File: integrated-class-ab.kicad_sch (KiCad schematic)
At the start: 35 parts, among them U10 CSA230PASOT235, U5 SL9062D, U9 LT1794

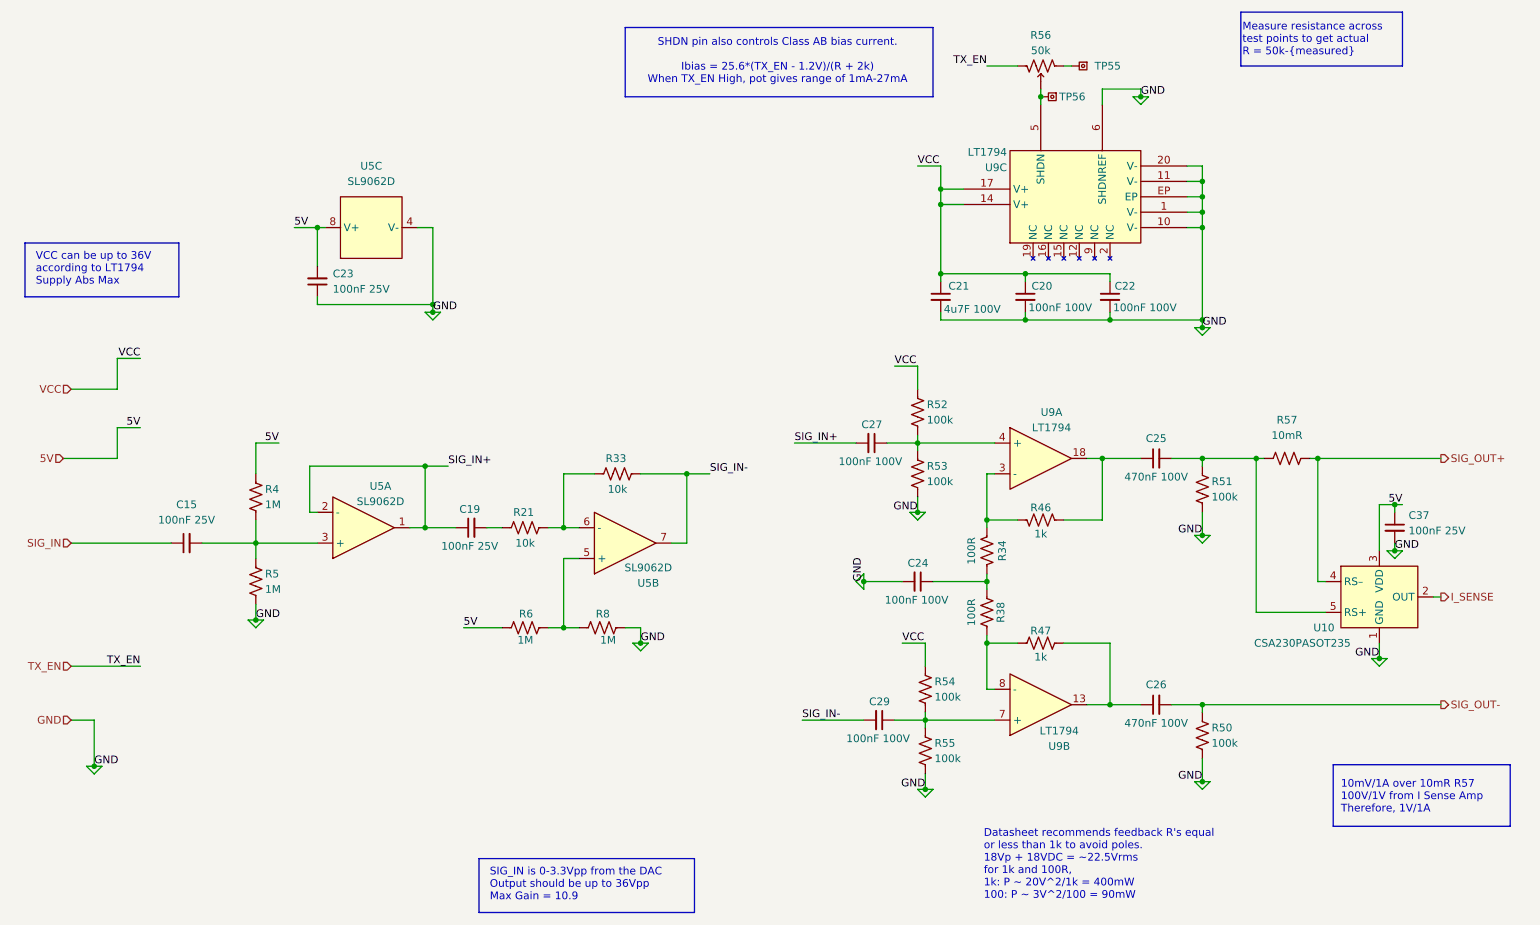
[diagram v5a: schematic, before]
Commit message: implementing feedback + added stepper driver
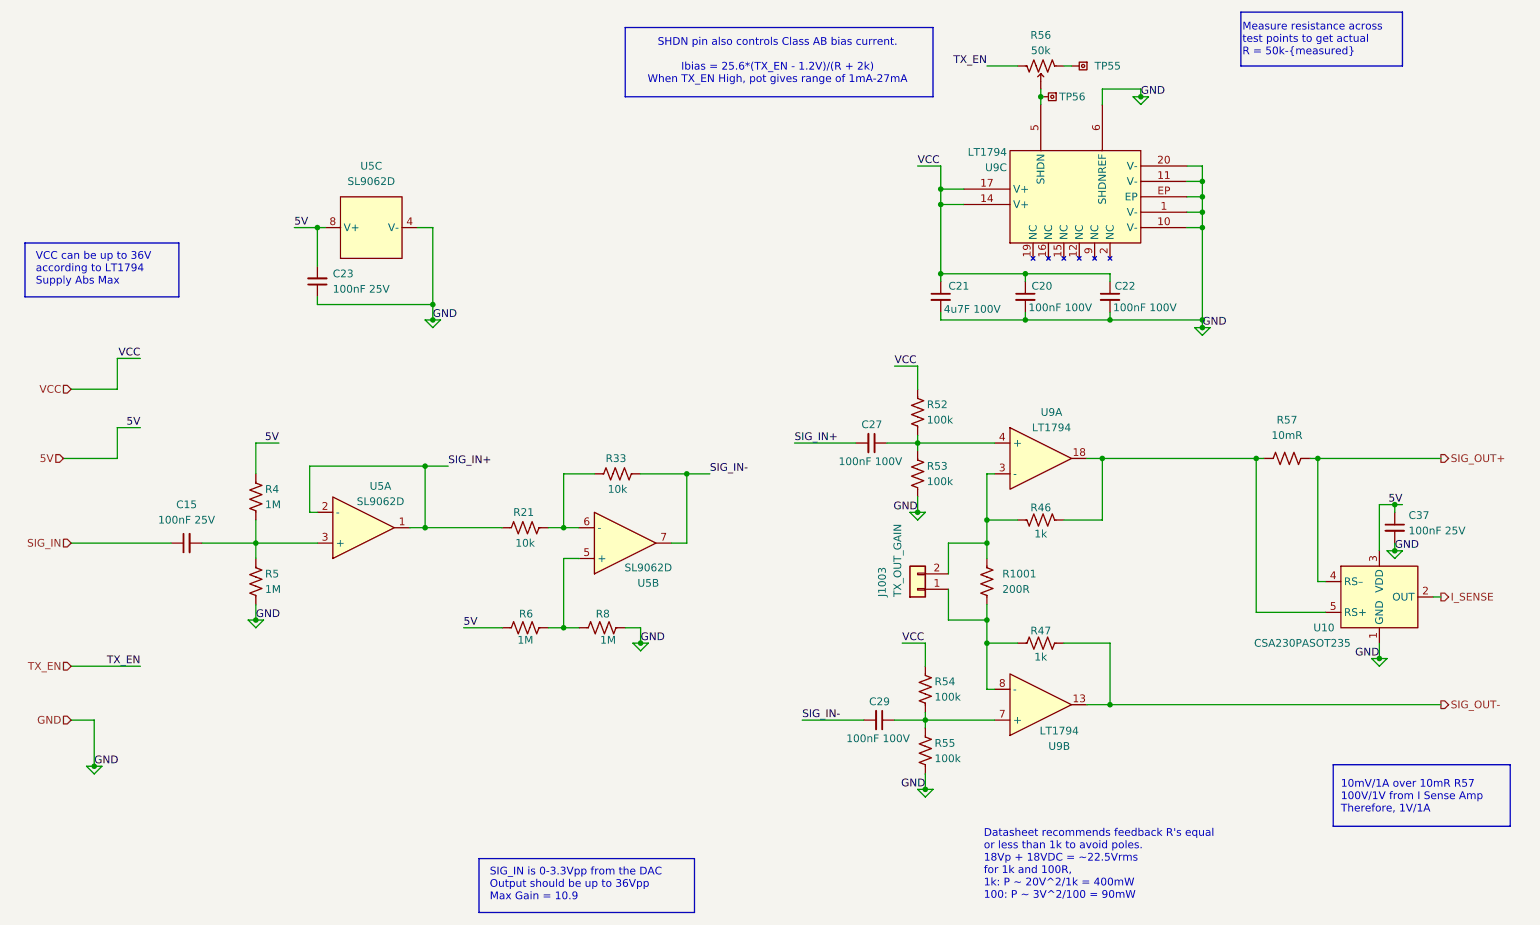
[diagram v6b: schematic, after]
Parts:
- removed C19: 100nF 25V, BR_Passives:C_0201_0603Metric-minimized, symbol BR_Capacitors_0201:C_0201_100nF_25V_X7R_10%
- removed C24: 100nF 100V, BR_Passives:C_0402_1005Metric-minimized, symbol BR_Capacitors_0402:C_0402_100nF_100V_X5R_20%
- removed C25, C26: 470nF 100V, BR_Passives:C_0805_2012Metric-minimized, symbol BR_Capacitors_0805:C_0805_470nF_100V_X7R_10%
- removed R34, R38: 100R, BR_Passives:R_0603_1608Metric, symbol BR_Resistors_0603:R_0603_100R
- removed R50, R51: 100k, BR_Passives:R_0201_0603Metric-minimized, symbol BR_Resistors_0201:R_0201_100k
- added J1003: TX_OUT_GAIN, BR_Connectors:PinHeader_1x02_P2.54mm_Vertical, symbol BR_Connectors_Header:Header_Socket_SIP_01x02_2.54mm_Vert_PTH
- added R1001: 200R, BR_Passives:C_0402_1005Metric-minimized, symbol BR_Resistors_0402:R_0402_200R
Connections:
- net SIG_IN+: now also R21.1
- net SIG_OUT-: now also R47.2, U9.13
- net at R47.1, U9.8 (-): now also J1003.1 (Pin_1), R1001.2
- net at R46.2, U9.3 (-): now also J1003.2 (Pin_2), R1001.1
- net at R46.1, U9.18: now also R57.1, U10.5 (RS+)

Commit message: completed feedback from review + reannotated sheets
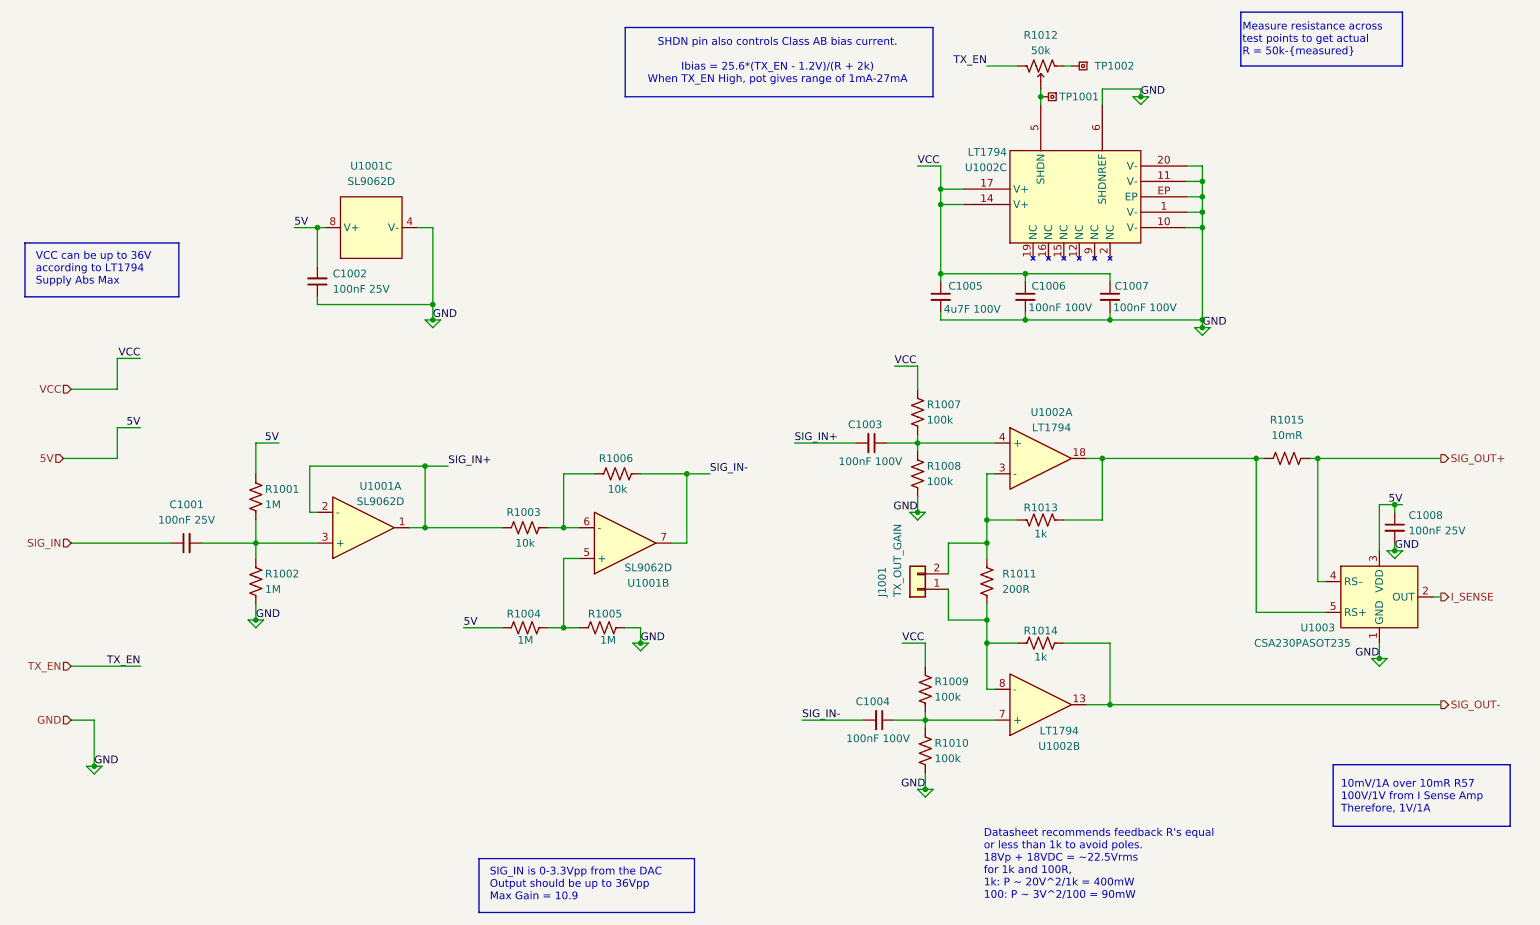
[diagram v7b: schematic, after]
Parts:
- renumbered C15 to C1001, C23 to C1002, C27 to C1003, C29 to C1004, C21 to C1005, C20 to C1006, C22 to C1007, C37 to C1008, J1003 to J1001, R4 to R1001, R5 to R1002, R21 to R1003, R6 to R1004, R8 to R1005, R33 to R1006, R52 to R1007, R53 to R1008, R54 to R1009, R55 to R1010, R1001 to R1011, R56 to R1012, R46 to R1013, R47 to R1014, R57 to R1015, TP56 to TP1001, TP55 to TP1002, U5 to U1001, U9 to U1002, U10 to U1003

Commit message: layout start
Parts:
- TP1002: value TP_SQUARE_TH_500um -> POT1; footprint POT1 -> BR_Virtual_Parts:TP_SQUARE_TH_1mm
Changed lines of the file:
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@@
 			)
 		)
-		(property "Value" "TP_SQUARE_TH_500um"
+		(property "Value" "POT1"
 			(at 205.4225 24.13 0)
 			(effects
@@
 			)
 		)
-		(property "Footprint" "POT1"
+		(property "Footprint" "BR_Virtual_Parts:TP_SQUARE_TH_1mm"
 			(at 214.376 22.86 0)
 			(effects
